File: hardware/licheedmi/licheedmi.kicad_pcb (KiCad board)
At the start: 4 copper layers, 94 x 38 mm, 75 parts, among them J1 Conn_01x09, J2 HDMI_A_PCB, J3 LicheePiNano_LCD, J4 HDMI_A, J5 USB_C_Receptacle_USB2.0, U1 TDA19988, U2 LicheeNano, U3 TS3DV20812, U4 SC6206B, U5 CH340C

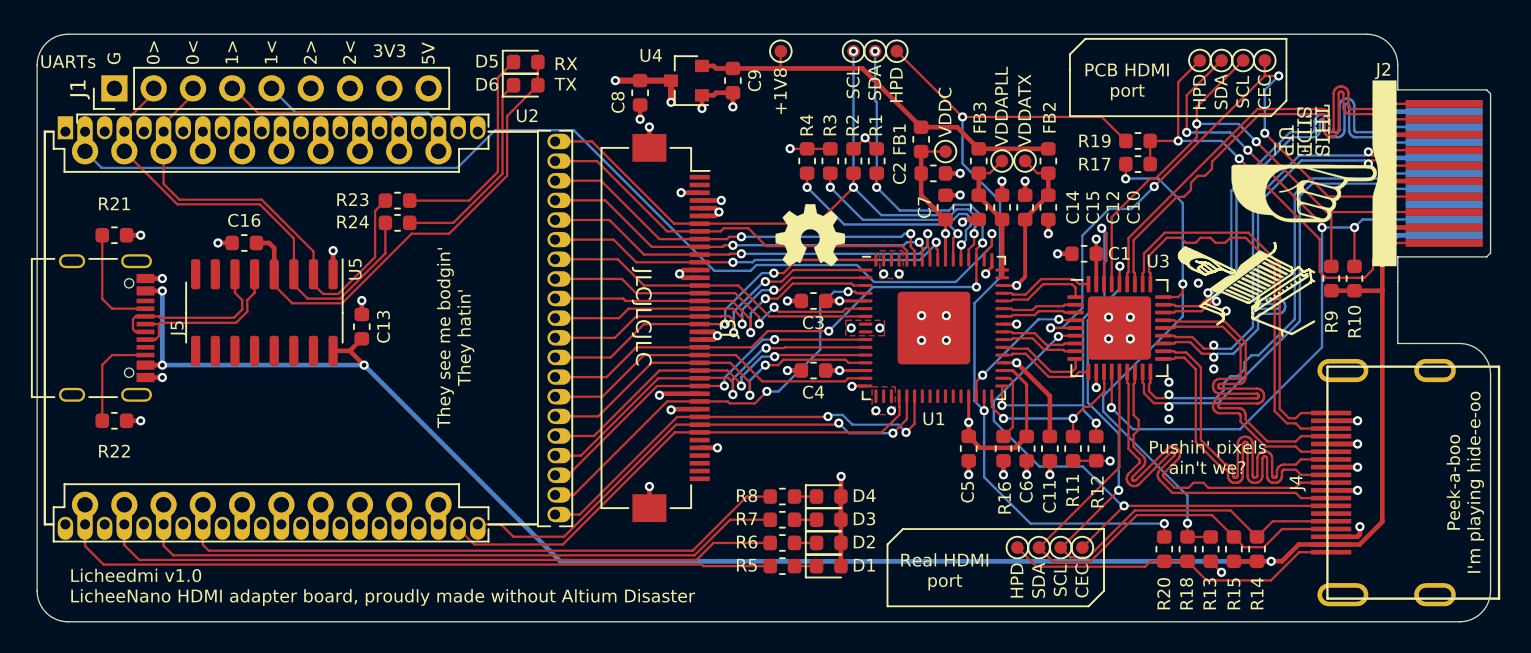
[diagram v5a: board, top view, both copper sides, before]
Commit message: pcb: Reroute PCB following footprint flip
Bowtie and complicated via thingies are gone now \o/
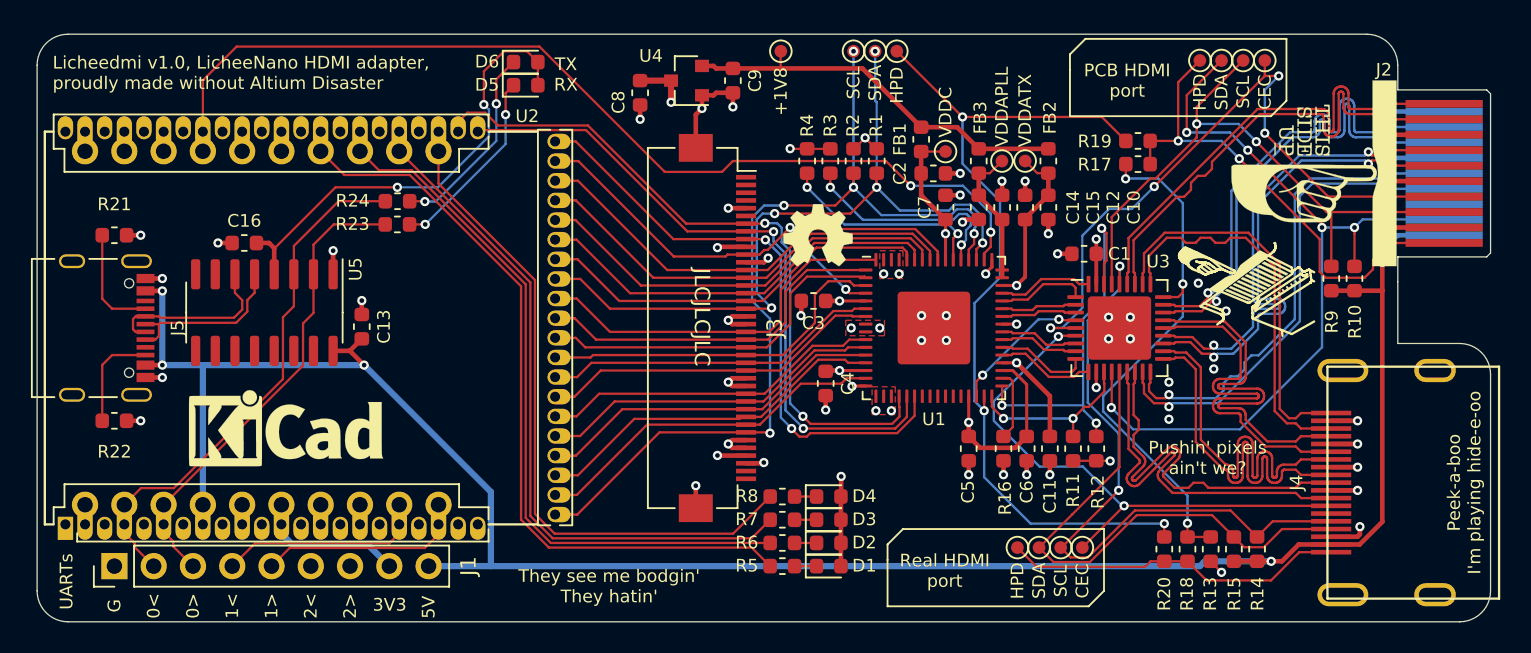
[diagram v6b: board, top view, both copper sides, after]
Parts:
- added REF**: KiCad-Logo_5mm_SilkScreen, Symbol:KiCad-Logo_5mm_SilkScreen, F.Cu at (91.1, 97.0)
- moved J1 30.9 mm to (80.0, 105.4)
- moved J3 3.00 mm to (119.0, 90.0)
- moved R23 1.54 mm to (98.3, 83.3)
- moved D5 1.50 mm to (106.6, 74.3)
- moved D6 1.50 mm to (106.6, 72.8)
- moved R24 1.40 mm to (98.3, 81.8)
- moved C4 1.15 mm to (126.0, 93.6), turned to 270 degrees
- moved REF** 0.50 mm to (125.5, 85.0)
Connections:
- J3 pad 10: /LCD_R5 -> +3V3
- J3 pad 11: /LCD_R6 -> /LCD_CLK
- J3 pad 12: /LCD_R7 -> GND
- J3 pad 13: GND -> /LCD_B7
- J3 pad 14: GND -> /LCD_B6
- J3 pad 15: /LCD_G2 -> /LCD_B5
- J3 pad 16: /LCD_G3 -> /LCD_B4
- J3 pad 17: /LCD_G4 -> /LCD_B3
- J3 pad 18: /LCD_G5 -> /CPU_SDA
- J3 pad 19: /LCD_G6 -> GND
- J3 pad 20: /LCD_G7 -> GND
- J3 pad 21: GND -> /LCD_G7
- J3 pad 22: GND -> /LCD_G6
- J3 pad 23: /CPU_SDA -> /LCD_G5
- J3 pad 24: /LCD_B3 -> /LCD_G4
- J3 pad 25: /LCD_B4 -> /LCD_G3
- J3 pad 26: /LCD_B5 -> /LCD_G2
- J3 pad 27: /LCD_B6 -> GND
- J3 pad 28: /LCD_B7 -> GND
- J3 pad 29: GND -> /LCD_R7
- J3 pad 3: GND -> Net-(J3-Pad3)
- J3 pad 30: /LCD_CLK -> /LCD_R6
- J3 pad 31: +3V3 -> /LCD_R5
- J3 pad 32: /LCD_HSYNC -> /LCD_R4
- J3 pad 33: /LCD_VSYNC -> /LCD_R3
- J3 pad 34: /LCD_DE -> /CPU_SCL
- J3 pad 35: Net-(J3-Pad35) -> GND
- J3 pad 37: Net-(J3-Pad37) -> +3V3
- J3 pad 38: Net-(J3-Pad38) -> GND
- J3 pad 4: +3V3 -> Net-(J3-Pad4)
- J3 pad 6: GND -> Net-(J3-Pad6)
- J3 pad 7: /CPU_SCL -> /LCD_DE
- J3 pad 8: /LCD_R3 -> /LCD_VSYNC
- J3 pad 9: /LCD_R4 -> /LCD_HSYNC
- U1 pad 10: /LCD_B7 -> /LCD_R7
- U1 pad 11: /LCD_B6 -> /LCD_R6
- U1 pad 12: /LCD_B5 -> /LCD_R5
- U1 pad 13: /LCD_B4 -> /LCD_R4
- U1 pad 15: /LCD_B3 -> /LCD_R3
- U1 pad 56: /LCD_R7 -> /LCD_B7
- U1 pad 57: /LCD_R6 -> /LCD_B6
- U1 pad 58: /LCD_R5 -> /LCD_B5
- U1 pad 59: /LCD_R4 -> /LCD_B4
- U1 pad 60: /LCD_R3 -> /LCD_B3
- U2 pad 2: /HDMI_INT -> Net-(U2-Pad2)
- U2 pad 45: Net-(U2-Pad45) -> /LED3
- U2 pad 47: Net-(U2-Pad47) -> /LED2
- U2 pad 49: Net-(U2-Pad49) -> /LED1
- U2 pad 51: Net-(U2-Pad51) -> /LED0
- U2 pad 57: /LED3 -> /HDMI_INT
- U2 pad 59: /LED2 -> Net-(U2-Pad59)
- U2 pad 61: /LED1 -> Net-(U2-Pad61)
- U2 pad 63: /LED0 -> Net-(U2-Pad63)
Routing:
- net /CPU_SCL: track 44.1 -> 59.6 mm, vias 3 -> 5
- net +5V: track 152.6 -> 139.5 mm
- net /LCD_DE: track 33.9 -> 45.6 mm, vias 0 -> 2
- net /LCD_HSYNC: track 28.4 -> 39.1 mm
- net /LCD_VSYNC: track 33.3 -> 43.8 mm
- net /LCD_B7: track 24.0 -> 29.4 mm, vias 2 -> 0
- net /LCD_R6: track 27.8 -> 22.5 mm, vias 2 -> 0
- net /LCD_R7: track 27.0 -> 22.1 mm, vias 2 -> 0
- net /HDMI_INT: track 68.1 -> 63.4 mm, vias 1 -> 2
- net /TX0: track 29.4 -> 33.8 mm
- net /LCD_B5: track 23.5 -> 27.7 mm, vias 2 -> 0
- net /LCD_B3: track 22.0 -> 25.9 mm
- net /LCD_B6: track 24.9 -> 28.5 mm, vias 2 -> 0
- net /LCD_R5: track 26.1 -> 22.8 mm, vias 2 -> 0
- net +3V3: track 128.3 -> 131.6 mm, vias 8 -> 7
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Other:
- board text added: "LCD_HSYNC LCD_CLK LCD_B7 LCD_B6 LCD_B5 LCD_B4 LCD_B3 CPU_SDA LCD_G7 LCD_G6 LCD_G5 LCD_G4 LCD_G3 LCD_G2 LCD_R7 LCD_R6 LCD_R5 LCD_R4 LCD_R3 CPU_SCL"
- board text added: "Licheedmi v1.0, LicheeNano HDMI adapter, proudly made without Altium Disaster"
- board text added: "TX RX"
- board text removed: "Licheedmi v1.0 LicheeNano HDMI adapter board, proudly made without Altium Disaster"
- board text removed: "RX TX"

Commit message: pcb: Add Lichee pinout on silk and stich grounds
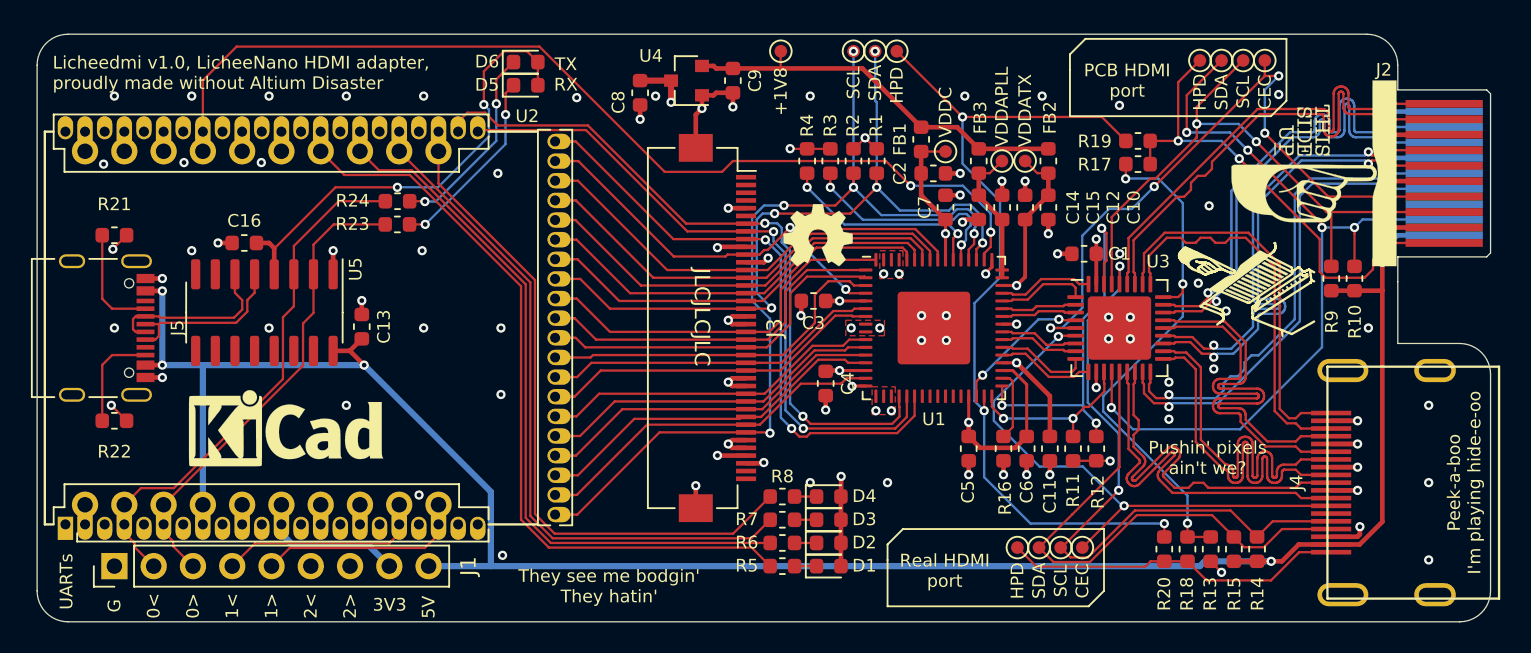
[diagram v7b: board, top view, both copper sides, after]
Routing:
- net +5V: track 139.5 -> 140.8 mm
- net Net-(U2-Pad63): track 0.00 -> 1.27 mm
- net Net-(U2-Pad61): track 0.00 -> 1.27 mm
- net Net-(U2-Pad59): track 0.00 -> 1.27 mm
- net Net-(U2-Pad2): track 0.00 -> 1.27 mm
- net Net-(U2-Pad16): track 0.00 -> 1.27 mm
- net Net-(U2-Pad14): track 0.00 -> 1.27 mm
- net /TX2: track 43.9 -> 45.1 mm
- net /TX1: track 12.3 -> 13.5 mm
- net /TX0: track 33.8 -> 35.0 mm
- net /RX1: track 12.3 -> 13.6 mm
- net /RX0: track 29.5 -> 30.8 mm
- net /LED3: track 42.8 -> 44.0 mm
- net /LED2: track 43.7 -> 45.0 mm
- net /LED1: track 45.9 -> 47.1 mm
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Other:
- rule trace_min: 0.15 -> 0
- board text added: "HPCOMFB HPCOM PA3 HPL PA2 HPR PA1 MICIN PA0 LINEIN 3V3 ~RST GND LRADC 5V AVCC PE0 TV_OUT PE1 USB_DP PE2 USB_DM"
- board text added: "LCD_VSYNC LCD_DE PE12 SDC0_D1 PE11 SDC0_D0 PE10 SDC0_CLK PE9 SDC0_CMD PE8 SDC0_D3 PE7 SDC0_D2 PE6 SPI0_CLK PE5 SPI0_CS PE4 SPI0_MISO PE3 SPI0_MOSI"

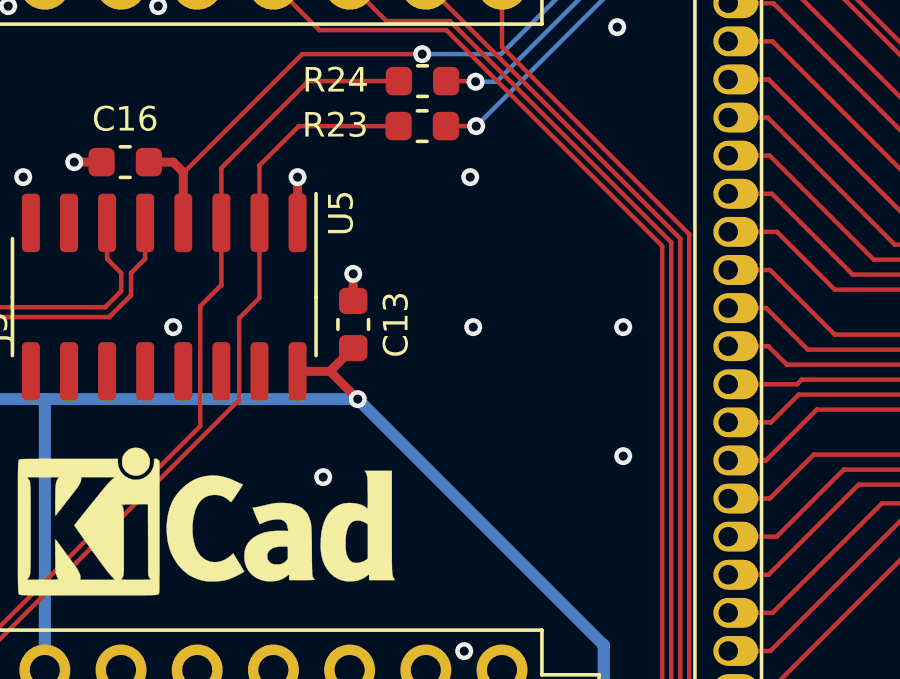
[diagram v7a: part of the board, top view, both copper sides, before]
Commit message: pcb: Add lichee orientation to silk
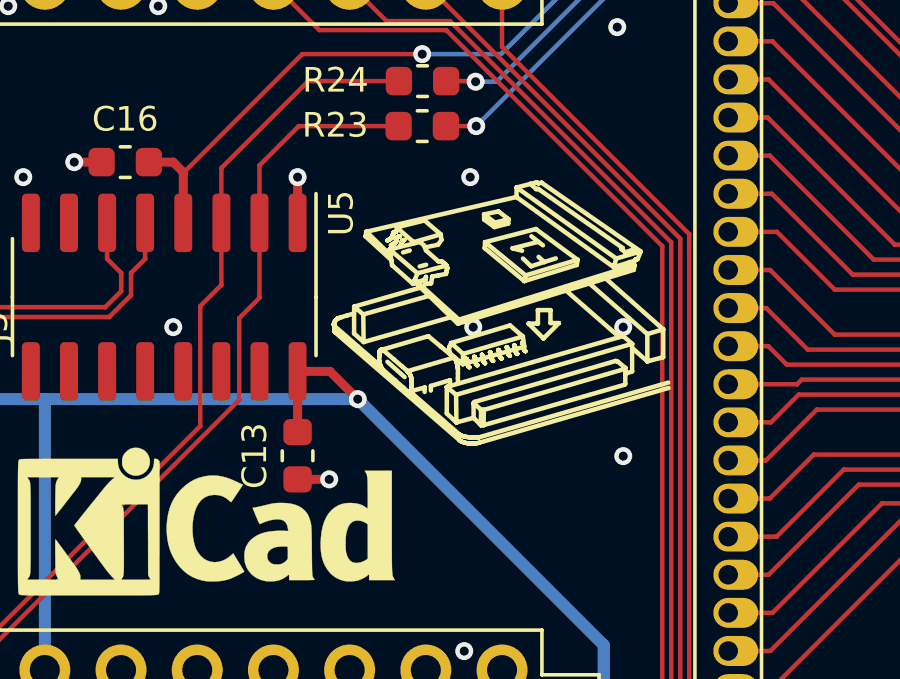
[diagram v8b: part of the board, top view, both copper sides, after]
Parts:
- moved C13 4.75 mm to (94.1, 94.3), turned to 90 degrees
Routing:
- net +5V: track 140.8 -> 141.7 mm
- net GND: track 73.5 -> 73.6 mm, vias 94 -> 93
